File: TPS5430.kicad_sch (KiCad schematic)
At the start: 38 parts, among them J1 Barrel_Jack, J2 Screw_Terminal_01x02, Q1 AO3401A, U1 TPS5430DDA

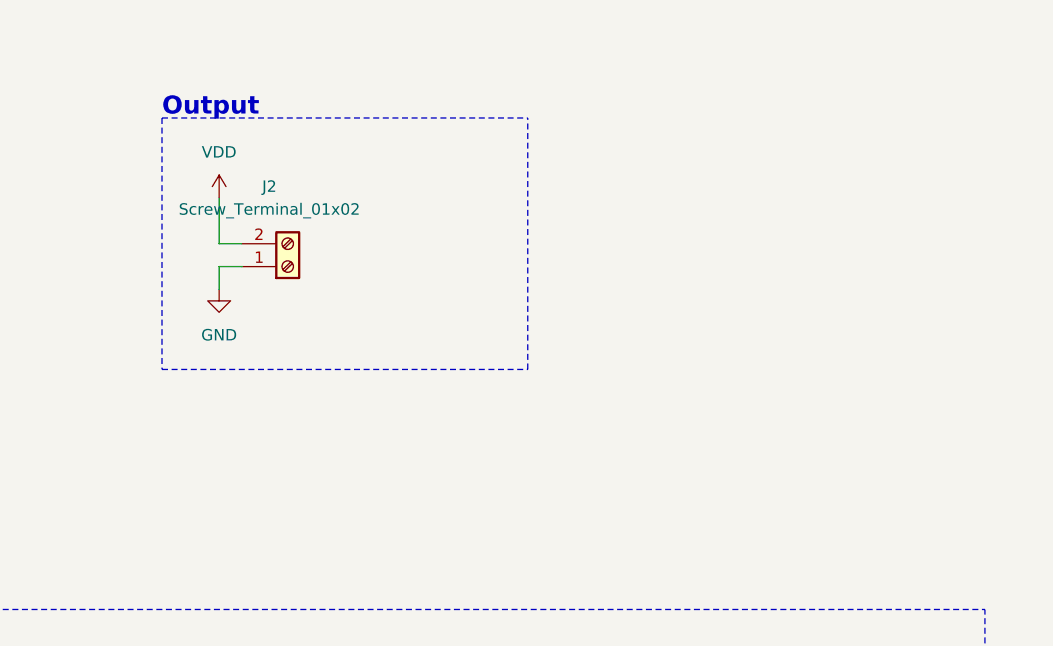
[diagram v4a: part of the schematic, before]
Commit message: Add Status LED
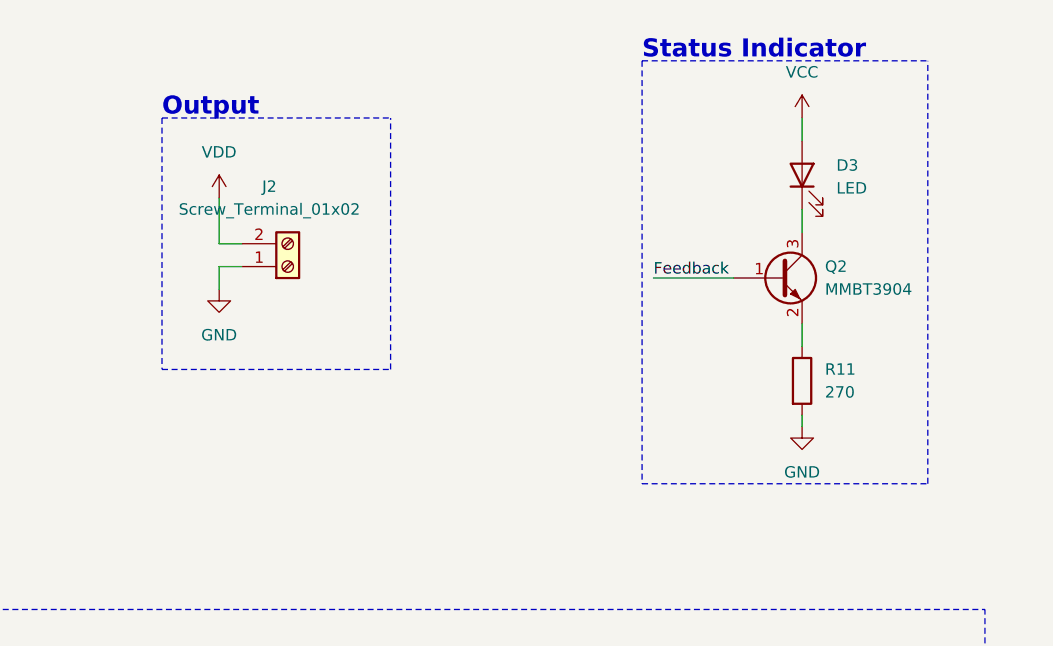
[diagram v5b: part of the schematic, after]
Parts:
- added D3: LED, LED_SMD:LED_0603_1608Metric, symbol Device:LED
- added Q2: MMBT3904, Package_TO_SOT_SMD:SOT-23, symbol Transistor_BJT:MMBT3904
- added R11: 270, Resistor_SMD:R_0603_1608Metric, symbol Device:R
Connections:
- net Feedback: now also Q2.1 (B)
- net GND: now also R11.2
- net VCC: now also D3.2 (A)
- new net: D3.1 (K), Q2.3 (C)
- new net: Q2.2 (E), R11.1
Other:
- note added: "Status Indicator"
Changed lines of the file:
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@@
+    (stroke (width 0) (type solid) (color 0 0 0 0))
+  )
+  (wire (pts (xy 240.03 55.88) (xy 248.92 55.88))
     (stroke (width 0) (type solid) (color 0 0 0 0))
   )
@@
   )
   (wire (pts (xy 240.03 144.78) (xy 240.03 146.05))
+    (stroke (width 0) (type solid) (color 0 0 0 0))
+  )
+  (wire (pts (xy 256.54 38.1) (xy 256.54 40.64))
+    (stroke (width 0) (type solid) (color 0 0 0 0))
+  )
+  (wire (pts (xy 256.54 48.26) (xy 256.54 50.8))
+    (stroke (width 0) (type solid) (color 0 0 0 0))
+  )
+  (wire (pts (xy 256.54 60.96) (xy 256.54 63.5))
+    (stroke (width 0) (type solid) (color 0 0 0 0))
+  )
+  (wire (pts (xy 256.54 71.12) (xy 256.54 72.39))
     (stroke (width 0) (type solid) (color 0 0 0 0))
   )
@@
     (stroke (width 0) (type dash) (color 0 0 0 0))
   )
-  (polyline (pts (xy 185.42 38.1) (xy 226.06 38.1))
+  (polyline (pts (xy 185.42 38.1) (xy 210.82 38.1))
     (stroke (width 0) (type dash) (color 0 0 0 0))
   )
-  (polyline (pts (xy 185.42 66.04) (xy 226.06 66.04))
+  (polyline (pts (xy 185.42 66.04) (xy 210.82 66.04))
     (stroke (width 0) (type dash) (color 0 0 0 0))
   )
-  (polyline (pts (xy 226.06 66.04) (xy 226.06 38.1))
+  (polyline (pts (xy 210.82 66.04) (xy 210.82 38.1))
+    (stroke (width 0) (type dash) (color 0 0 0 0))
+  )
+  (polyline (pts (xy 238.76 31.75) (xy 238.76 78.74))
+    (stroke (width 0) (type dash) (color 0 0 0 0))
+  )
+  (polyline (pts (xy 238.76 31.75) (xy 270.51 31.75))
+    (stroke (width 0) (type dash) (color 0 0 0 0))
+  )
+  (polyline (pts (xy 238.76 78.74) (xy 270.51 78.74))
+    (stroke (width 0) (type dash) (color 0 0 0 0))
+  )
+  (polyline (pts (xy 270.51 78.74) (xy 270.51 31.75))
     (stroke (width 0) (type dash) (color 0 0 0 0))
   )
@@
     (effects (font (size 1.27 1.27) (thickness 0.254) bold) (justify left bottom))
   )
+  (text "Status Indicator" (at 238.76 31.75 0)
+    (effects (font (size 2 2) (thickness 0.4) bold) (justify left bottom))
+  )
   (text "1V8" (at 252.73 121.92 0)
     (effects (font (size 1.27 1.27) (thickness 0.254) bold) (justify left bottom))
@@
     (effects (font (size 1.27 1.27)) (justify left bottom))
   )
+  (label "Feedback" (at 240.03 55.88 0)
+    (effects (font (size 1.27 1.27)) (justify left bottom))
+  )
   (symbol (lib_id "power:VCC") (at 26.67 110.49 0) (unit 1)
     (in_bom yes) (on_board yes) (fields_autoplaced)
@@
     )
     (property "Datasheet" "" (id 3) (at 213.36 102.87 0)
+      (effects (font (size 1.27 1.27)) hide)
+    )
+    (pin "1")
+  )
+  (symbol (lib_id "power:VCC") (at 256.54 38.1 0) (unit 1)
+    (in_bom yes) (on_board yes) (fields_autoplaced)
+    (property "Reference" "#PWR01" (id 0) (at 256.54 41.91 0)
+      (effects (font (size 1.27 1.27)) hide)
+    )
+    (property "Value" "VCC" (id 1) (at 256.54 33.02 0))
+    (property "Footprint" "" (id 2) (at 256.54 38.1 0)
+      (effects (font (size 1.27 1.27)) hide)
+    )
+    (property "Datasheet" "" (id 3) (at 256.54 38.1 0)
       (effects (font (size 1.27 1.27)) hide)
     )
@@
     )
     (property "Datasheet" "" (id 3) (at 240.03 146.05 0)
+      (effects (font (size 1.27 1.27)) hide)
+    )
+    (pin "1")
+  )
+  (symbol (lib_id "power:GND") (at 256.54 72.39 0) (unit 1)
+    (in_bom yes) (on_board yes) (fields_autoplaced)
+    (property "Reference" "#PWR02" (id 0) (at 256.54 78.74 0)
+      (effects (font (size 1.27 1.27)) hide)
+    )
+    (property "Value" "GND" (id 1) (at 256.54 77.47 0))
+    (property "Footprint" "" (id 2) (at 256.54 72.39 0)
+      (effects (font (size 1.27 1.27)) hide)
+    )
+    (property "Datasheet" "" (id 3) (at 256.54 72.39 0)
       (effects (font (size 1.27 1.27)) hide)
     )
@@
     (pin "2")
   )
+  (symbol (lib_id "Device:R") (at 256.54 67.31 0) (unit 1)
+    (in_bom yes) (on_board yes) (fields_autoplaced)
+    (property "Reference" "R11" (id 0) (at 259.08 66.0399 0)
+      (effects (font (size 1.27 1.27)) (justify left))
+    )
+    (property "Value" "270" (id 1) (at 259.08 68.5799 0)
+      (effects (font (size 1.27 1.27)) (justify left))
+    )
+    (property "Footprint" "Resistor_SMD:R_0603_1608Metric" (id 2) (at 254.762 67.31 90)
+      (effects (font (size 1.27 1.27)) hide)
+    )
+    (property "Datasheet" "https://datasheet.lcsc.com/lcsc/1811081711_UNI-ROYAL-Uniroyal-Elec-0603WAF2700T5E_C22966.pdf" (id 3) (at 256.54 67.31 0)
+      (effects (font (size 1.27 1.27)) hide)
+    )
+    (property "MPN" "0603WAF2700T5E" (id 4) (at 256.54 67.31 0)
+      (effects (font (size 1.27 1.27)) hide)
+    )
+    (property "Manufacturer" "UNI-ROYAL(Uniroyal Elec)" (id 5) (at 256.54 67.31 0)
+      (effects (font (size 1.27 1.27)) hide)
+    )
+    (property "Notes" "270Ω ±1% 0.1W ±100ppm/℃ 0603 Chip Resistor - Surface Mount RoHS" (id 6) (at 256.54 67.31 0)
+      (effects (font (size 1.27 1.27)) hide)
+    )
+    (property "LCSC" "C22966" (id 7) (at 256.54 67.31 0)
+      (effects (font (size 1.27 1.27)) hide)
+    )
+    (property "JLC" "0603" (id 8) (at 256.54 67.31 0)
+      (effects (font (size 1.27 1.27)) hide)
+    )
+    (pin "1")
+    (pin "2")
+  )
   (symbol (lib_id "Device:R") (at 257.81 135.89 0) (unit 1)
     (in_bom yes) (on_board yes) (fields_autoplaced)
@@
     (pin "2")
   )
+  (symbol (lib_id "Device:LED") (at 256.54 44.45 90) (unit 1)
+    (in_bom yes) (on_board yes) (fields_autoplaced)
+    (property "Reference" "D3" (id 0) (at 260.35 43.3704 90)
+      (effects (font (size 1.27 1.27)) (justify right))
+    )
+    (property "Value" "LED" (id 1) (at 260.35 45.9104 90)
+      (effects (font (size 1.27 1.27)) (justify right))
+    )
+    (property "Footprint" "LED_SMD:LED_0603_1608Metric" (id 2) (at 256.54 44.45 0)
+      (effects (font (size 1.27 1.27)) hide)
+    )
+    (property "Datasheet" "https://datasheet.lcsc.com/lcsc/1811101510_Everlight-Elec-19-217-GHC-YR1S2-3T_C72043.pdf" (id 3) (at 256.54 44.45 0)
+      (effects (font (size 1.27 1.27)) hide)
+    )
+    (property "MPN" "19-217/GHC-YR1S2/3T" (id 4) (at 256.54 44.45 0)
+      (effects (font (size 1.27 1.27)) hide)
+    )
+    (property "Manufacturer" "Everlight Elec" (id 5) (at 256.54 44.45 0)
+      (effects (font (size 1.27 1.27)) hide)
+    )
+    (property "Notes" "Green 520~535nm 0603 Light Emitting Diodes (LED) RoHS" (id 6) (at 256.54 44.45 0)
+      (effects (font (size 1.27 1.27)) hide)
+    )
+    (property "LCSC" "C72043" (id 7) (at 256.54 44.45 0)
+      (effects (font (size 1.27 1.27)) hide)
+    )
+    (pin "1")
+    (pin "2")
+  )
   (symbol (lib_id "Connector:Screw_Terminal_01x02") (at 199.39 54.61 0) (mirror x) (unit 1)
     (in_bom yes) (on_board yes) (fields_autoplaced)
@@
     )
     (property "JLC" "SMD" (id 8) (at 66.04 44.45 0)
+      (effects (font (size 1.27 1.27)) hide)
+    )
+    (pin "1")
+    (pin "2")
+    (pin "3")
+  )
+  (symbol (lib_id "Transistor_BJT:MMBT3904") (at 254 55.88 0) (unit 1)
+    (in_bom yes) (on_board yes) (fields_autoplaced)
+    (property "Reference" "Q2" (id 0) (at 259.08 54.6099 0)
+      (effects (font (size 1.27 1.27)) (justify left))
+    )
+    (property "Value" "MMBT3904" (id 1) (at 259.08 57.1499 0)
+      (effects (font (size 1.27 1.27)) (justify left))
+    )
+    (property "Footprint" "Package_TO_SOT_SMD:SOT-23" (id 2) (at 259.08 57.785 0)
+      (effects (font (size 1.27 1.27) italic) (justify left) hide)
+    )
+    (property "Datasheet" "https://www.onsemi.com/pub/Collateral/2N3903-D.PDF" (id 3) (at 254 55.88 0)
+      (effects (font (size 1.27 1.27)) (justify left) hide)
+    )
+    (property "MPN" "MMBT3904" (id 4) (at 254 55.88 0)
+      (effects (font (size 1.27 1.27)) hide)
+    )
+    (property "Manufacturer" "Changjiang Electronics Tech (CJ)" (id 5) (at 254 55.88 0)
+      (effects (font (size 1.27 1.27)) hide)
+    )
+    (property "Notes" "Transistors (NPN/PNP) NPN 200mA 40V SOT-23(SOT-23-3) RoHS" (id 6) (at 254 55.88 0)
+      (effects (font (size 1.27 1.27)) hide)
+    )
+    (property "LCSC" "C20526" (id 7) (at 254 55.88 0)
       (effects (font (size 1.27 1.27)) hide)
     )
@@
       (reference "#FLG0102") (unit 1) (value "PWR_FLAG") (footprint "")
     )
+    (path "/7b1cb44a-84d8-4d38-a1fb-4c3cdf46580f"
+      (reference "#PWR01") (unit 1) (value "VCC") (footprint "")
+    )
+    (path "/745591fb-e924-490e-a037-5565f849fe88"
+      (reference "#PWR02") (unit 1) (value "GND") (footprint "")
+    )
     (path "/6c5e7e13-cb66-4fc5-ae71-99c5632d3cde"
       (reference "#PWR0101") (unit 1) (value "GND") (footprint "")
@@
       (reference "D2") (unit 1) (value "ZMM5V6") (footprint "Diode_SMD:D_MiniMELF")
     )
+    (path "/00cdb4c2-a038-4d1b-862a-03ad707639ba"
+      (reference "D3") (unit 1) (value "LED") (footprint "LED_SMD:LED_0603_1608Metric")
+    )
     (path "/324d0e2e-5b56-4ba6-93e5-47d464718235"
       (reference "F1") (unit 1) (value "Polyfuse") (footprint "Fuse:Fuse_1206_3216Metric")
@@
       (reference "Q1") (unit 1) (value "AO3401A") (footprint "Package_TO_SOT_SMD:SOT-23")
     )
+    (path "/409c8fca-54a5-42c6-b61e-f9bc4707fe3a"
+      (reference "Q2") (unit 1) (value "MMBT3904") (footprint "Package_TO_SOT_SMD:SOT-23")
+    )
     (path "/5171bfb3-95e8-436c-ba35-35c2d7ddce70"
       (reference "R1") (unit 1) (value "12k") (footprint "Resistor_SMD:R_0402_1005Metric")
@@
       (reference "R10") (unit 1) (value "120") (footprint "Resistor_SMD:R_0402_1005Metric")
     )
+    (path "/96239c57-f07b-4e98-8e16-76896743074e"
+      (reference "R11") (unit 1) (value "270") (footprint "Resistor_SMD:R_0603_1608Metric")
+    )
     (path "/62c79e30-4f04-449c-9719-4abace1da225"

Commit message: Add status LED & fix reverse polarity protection
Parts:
- C8: value 100n/16V -> 4n7/50V; LCSC C1525 -> C1538; MPN CL05B104KO5NNNC -> 0402B472K500NT; Manufacturer Samsung Electro-Mechanics -> FH(Guangdong Fenghua Advanced Tech); Notes 100nF ±10% 16V X7R 0402 Multilayer Ceramic Capacitors MLCC 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 -> 4.7nF ±10% 50V X7R 0402 Multilayer Ceramic Capacitors MLCC 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
- D3: JLC (none) -> LED_0603
- Q2: JLC (none) -> SOT-23-3
- R1: value 12k -> 100k; LCSC C25752 -> C25741; MPN 0402WGF1202TCE -> 0402WGF1003TCE; Notes 12kΩ ±1% 1/16W ±100ppm/℃ 0402 Chip Resistor - Surface Mount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 -> 100kΩ ±1% 1/16W ±100ppm/℃ 0402 Chip Resistor - Surface Moun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
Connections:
- net GND: now also C8.2
- net VCC: no longer C8.1
- net at D2.2 (A), Q1.1 (G), R1.1: now also C8.1; no longer C8.2
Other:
- moved on the sheet: C8, D2, R1

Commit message: Dim status LED and update to KiCAD 6
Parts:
- R11: value 270 -> 10k; LCSC C22966 -> C25804; MPN 0603WAF2700T5E -> 0603WAF1002T5E; Notes 270Ω ±1% 0.1W ±100ppm/℃ 0603 Chip Resistor - Surface Mount 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 -> ±1% 1/10W Thick Film Resistors 75V ±100ppm/℃ -55℃~+155℃ 10k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
